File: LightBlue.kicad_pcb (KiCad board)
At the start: 2 copper layers, 120 x 120 mm, 0 parts

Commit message: Initial layout with footprint placements
Signed-off-by: Stefan Agner <stefan@agner.ch>
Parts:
- added BT1: Battery_Cell, Battery:BatteryHolder_Keystone_1060_1x2032, F.Cu at (49.6, 90.2)
- added C1: 100n, Capacitor_SMD:C_0402_1005Metric, F.Cu at (92.4, 52.2)
- added C10: 18p, Capacitor_SMD:C_0402_1005Metric, F.Cu at (96.1, 50.2)
- added C11: 100n, Capacitor_SMD:C_0402_1005Metric, F.Cu at (92.6, 54.6)
- added C12: 10u, Capacitor_SMD:C_0805_2012Metric, F.Cu at (103.6, 51.6)
- added C13: 100n, Capacitor_SMD:C_0402_1005Metric, F.Cu at (103.1, 58.6)
- added C14: 100n/1kV, Capacitor_SMD:C_1206_3216Metric, F.Cu at (78.2, 37.4)
- added C15: 100u, Capacitor_Tantalum_SMD:CP_EIA-7343-31_Kemet-D, F.Cu at (83.6, 44.0)
- added C16: 10u, Capacitor_SMD:C_0805_2012Metric, F.Cu at (77.8, 62.9)
- added C17: 10u, Capacitor_SMD:C_0805_2012Metric, F.Cu at (103.6, 49.4)
- added C18: 100n, Capacitor_SMD:C_0402_1005Metric, F.Cu at (81.5, 62.1)
- added C19: 100n, Capacitor_SMD:C_0402_1005Metric, F.Cu at (119.9, 58.0)
- added C2: 100n, Capacitor_SMD:C_0402_1005Metric, F.Cu at (95.4, 58.2)
- added C20: 10u, Capacitor_SMD:C_0805_2012Metric, F.Cu at (119.3, 53.5)
- added C21: 100n, Capacitor_SMD:C_0402_1005Metric, F.Cu at (119.9, 56.0)
- added C22: 10u, Capacitor_SMD:C_0805_2012Metric, F.Cu at (123.7, 56.5)
- added C23: 2u2/25V, Capacitor_SMD:C_0402_1005Metric, F.Cu at (110.4, 56.5)
- added C24: 2u2/25V, Capacitor_SMD:C_0402_1005Metric, F.Cu at (107.9, 56.5)
- added C25: 100n, Capacitor_SMD:C_0402_1005Metric, F.Cu at (117.0, 56.0)
- added C26: 100n, Capacitor_SMD:C_0402_1005Metric, F.Cu at (108.6, 46.2)
- added C27: 100n, Capacitor_SMD:C_0402_1005Metric, F.Cu at (117.0, 58.0)
- added C28: 100n, Capacitor_SMD:C_0402_1005Metric, F.Cu at (75.6, 57.0)
- added C29: 100n/1kV, Capacitor_SMD:C_1206_3216Metric, F.Cu at (62.3, 55.3)
- added C3: 100n, Capacitor_SMD:C_0402_1005Metric, F.Cu at (99.6, 52.6)
- added C30: 100n, Capacitor_SMD:C_0402_1005Metric, F.Cu at (138.4, 111.0)
- added C31: 100n, Capacitor_SMD:C_0402_1005Metric, F.Cu at (136.0, 136.0)
- added C32: 100n, Capacitor_SMD:C_0402_1005Metric, F.Cu at (135.3, 111.0)
- added C33: 33u/35V, Capacitor_Tantalum_SMD:CP_EIA-7343-31_Kemet-D, F.Cu at (6.74, 22.9)
- added C34: 33u/35V, Capacitor_Tantalum_SMD:CP_EIA-7343-31_Kemet-D, F.Cu at (-9.36, 35.5)
- added C35: 33u/35V, Capacitor_Tantalum_SMD:CP_EIA-7343-31_Kemet-D, F.Cu at (-10.3, 43.3)
- added C36: 10u/35V, Capacitor_SMD:C_0805_2012Metric, F.Cu at (6.24, 33.4)
- added C37: 33u/35V, Capacitor_Tantalum_SMD:CP_EIA-7343-31_Kemet-D, F.Cu at (-3.15, 22.9)
- added C38: 10u/35V, Capacitor_SMD:C_0805_2012Metric, F.Cu at (-3.17, 40.0)
- added C39: 100n/35V, Capacitor_SMD:C_0402_1005Metric, F.Cu at (-12.4, 54.8)
- added C4: 100n, Capacitor_SMD:C_0402_1005Metric, F.Cu at (99.6, 57.4)
- added C40: 100n/35V, Capacitor_SMD:C_0402_1005Metric, F.Cu at (-19.3, 62.5)
- added C41: 10n, Capacitor_SMD:C_0402_1005Metric, F.Cu at (-20.9, 65.5)
- added C42: 100n/35V, Capacitor_SMD:C_0402_1005Metric, F.Cu at (12.8, 31.5)
- added C43: 100n/35V, Capacitor_SMD:C_0402_1005Metric, F.Cu at (5.45, 37.9)
- added C44: 10n, Capacitor_SMD:C_0402_1005Metric, F.Cu at (16.6, 28.5)
- added C45: 47p, Capacitor_SMD:C_0402_1005Metric, F.Cu at (9.90, 33.5)
- added C46: 1n2, Capacitor_SMD:C_0402_1005Metric, F.Cu at (-5.80, 49.2)
- added C47: 47p, Capacitor_SMD:C_0402_1005Metric, F.Cu at (9.90, 31.5)
- added C48: 1n2, Capacitor_SMD:C_0402_1005Metric, F.Cu at (-12.4, 56.7)
- added C49: 47p, Capacitor_SMD:C_0402_1005Metric, F.Cu at (-23.7, 65.5)
- added C5: 1u, Capacitor_SMD:C_0402_1005Metric, F.Cu at (92.8, 58.4)
- added C50: 47p, Capacitor_SMD:C_0402_1005Metric, F.Cu at (-1.05, 44.4)
- added C51: 100n, Capacitor_SMD:C_0402_1005Metric, F.Cu at (-1.05, 42.5)
- added C52: 100n, Capacitor_SMD:C_0402_1005Metric, F.Cu at (-23.7, 67.4)
- added C53: 10u, Capacitor_SMD:C_0805_2012Metric, F.Cu at (3.99, 27.4)
- added C54: 10u, Capacitor_SMD:C_0805_2012Metric, F.Cu at (12.9, 29.1)
- added C55: 10u, Capacitor_SMD:C_0805_2012Metric, F.Cu at (8.44, 27.4)
- added C56: 10u, Capacitor_SMD:C_0805_2012Metric, F.Cu at (-18.5, 60.0)
- added C57: 10u, Capacitor_SMD:C_0805_2012Metric, F.Cu at (6.24, 30.4)
- added C58: 100u, Capacitor_Tantalum_SMD:CP_EIA-7343-31_Kemet-D, F.Cu at (-20.2, 49.1)
- added C59: 10u, Capacitor_SMD:C_0805_2012Metric, F.Cu at (-22.9, 60.0)
- added C6: 1u, Capacitor_SMD:C_0402_1005Metric, F.Cu at (97.8, 58.4)
- added C60: 100u, Capacitor_Tantalum_SMD:CP_EIA-7343-31_Kemet-D, F.Cu at (-3.15, 28.8)
- added C61: 100u, Capacitor_Tantalum_SMD:CP_EIA-7343-31_Kemet-D, F.Cu at (-20.2, 43.3)
- added C62: 100n, Capacitor_SMD:C_0402_1005Metric, F.Cu at (67.0, 140.5)
- added C63: 1u/35V, Capacitor_SMD:C_0402_1005Metric, F.Cu at (52.0, 138.5)
- added C64: 100n/35v, Capacitor_SMD:C_0402_1005Metric, F.Cu at (60.0, 138.5)
- added C65: 100n, Capacitor_SMD:C_0402_1005Metric, F.Cu at (72.1, 106.1)
- added C66: 1u, Capacitor_SMD:C_0402_1005Metric, F.Cu at (102.8, 137.9)
- added C67: 100n, Capacitor_SMD:C_0402_1005Metric, F.Cu at (113.0, 139.6)
- added C68: 100n, Capacitor_SMD:C_0402_1005Metric, F.Cu at (102.8, 140.4)
- added C69: 10u, Capacitor_SMD:C_0805_2012Metric, F.Cu at (130.8, 55.6)
- added C7: 100n, Capacitor_SMD:C_0402_1005Metric, F.Cu at (90.4, 59.2)
- added C70: 2n2/100V, Capacitor_SMD:C_0805_2012Metric, F.Cu at (190.7, 78.6)
- added C71: 1n/100V, Capacitor_SMD:C_0805_2012Metric, F.Cu at (182.1, 83.9)
- added C72: 1n/100V, Capacitor_SMD:C_0805_2012Metric, F.Cu at (200.3, 68.2)
- added C73: 47n/100V, Capacitor_SMD:C_0805_2012Metric, F.Cu at (209.3, 60.2)
- added C74: 100n/100V, Capacitor_SMD:C_0805_2012Metric, F.Cu at (182.1, 86.9)
- added C75: 100n/100V, Capacitor_SMD:C_0805_2012Metric, F.Cu at (215.3, 52.5)
- added C76: 100n/100V, Capacitor_SMD:C_0805_2012Metric, F.Cu at (194.1, 74.6)
- added C77: 100n/100V, Capacitor_SMD:C_0805_2012Metric, F.Cu at (209.3, 57.2)
- added C78: 100n/100V, Capacitor_SMD:C_0805_2012Metric, F.Cu at (176.2, 90.6)
- added C79: 100n/100V, Capacitor_SMD:C_0805_2012Metric, F.Cu at (200.3, 71.2)
- added C8: 4u7, Capacitor_SMD:C_0402_1005Metric, F.Cu at (99.6, 55.0)
- added C80: 47u/63V, Capacitor_SMD:C_0805_2012Metric, F.Cu at (186.6, 83.2)
- added C81: 2u2/100V, Capacitor_SMD:C_0805_2012Metric, F.Cu at (203.2, 63.6)
- added C82: 2u2/100V, Capacitor_SMD:C_0805_2012Metric, F.Cu at (187.8, 51.3)
- added C83: 47p/100V, Capacitor_SMD:C_0805_2012Metric, F.Cu at (223.6, 46.1)
- added C84: 2u2/100V, Capacitor_SMD:C_0805_2012Metric, F.Cu at (217.8, 49.5)
- added C85: 47n/100V, Capacitor_SMD:C_0805_2012Metric, F.Cu at (215.3, 55.5)
- added C86: 68n/100V, Capacitor_SMD:C_0805_2012Metric, F.Cu at (173.4, 95.2)
- added C87: 1n, Capacitor_SMD:C_0402_1005Metric, F.Cu at (184.3, 89.7)
- added C88: 1u, Capacitor_SMD:C_0402_1005Metric, F.Cu at (184.3, 91.6)
- added C89: 1n, Capacitor_SMD:C_0402_1005Metric, F.Cu at (188.7, 85.7)
- added C9: 18p, Capacitor_SMD:C_0402_1005Metric, F.Cu at (90.9, 49.7)
- added C90: 22n, Capacitor_SMD:C_0402_1005Metric, F.Cu at (197.3, 78.2)
- added C91: 100p, Capacitor_SMD:C_0402_1005Metric, F.Cu at (211.3, 62.7)
- added C92: 100u/35V, Capacitor_Tantalum_SMD:CP_EIA-7343-31_Kemet-D, F.Cu at (170.7, 78.5)
- added C93: 33u/35V, Capacitor_Tantalum_SMD:CP_EIA-7343-31_Kemet-D, F.Cu at (202.3, 40.9)
- added D1: LED_Small, LED_SMD:LED_0603_1608Metric, F.Cu at (120.8, 146.0)
- added D10: B2100-13-F, Diode_SMD:D_SMB, F.Cu at (192.3, 64.3)
- added D11: B2100-13-F, Diode_SMD:D_SMB, F.Cu at (169.9, 84.2)
- added D12: B2100-13-F, Diode_SMD:D_SMB, F.Cu at (194.8, 52.5)
- added D13: B2100-13-F, Diode_SMD:D_SMB, F.Cu at (203.2, 51.8)
- added D14: B2100-13-F, Diode_SMD:D_SMB, F.Cu at (211.4, 40.7)
- added D15: B2100-13-F, Diode_SMD:D_SMB, F.Cu at (184.0, 64.3)
- added D16: B2100-13-F, Diode_SMD:D_SMB, F.Cu at (211.4, 46.2)
- added D17: SMBJ58A-13-F, Diode_SMD:D_SMB, F.Cu at (179.8, 79.7)
- added D18: B3100-13-F, Diode_SMD:D_SMC, F.Cu at (185.2, 57.6)
- added D19: BAT41ZFILM, Diode_SMD:D_SOD-123, F.Cu at (177.0, 87.5)
- added D2: B3100-13-F, Diode_SMD:D_SMC, F.Cu at (-19.8, 36.5)
- added D20: BAT41ZFILM, Diode_SMD:D_SOD-123, F.Cu at (186.9, 75.5)
- added D21: BAT41ZFILM, Diode_SMD:D_SOD-123, F.Cu at (218.5, 46.3)
- added D22: BAT41ZFILM, Diode_SMD:D_SOD-123, F.Cu at (210.2, 50.7)
- added D23: BAT41ZFILM, Diode_SMD:D_SOD-123, F.Cu at (177.0, 84.1)
- added D24: B3100-13-F, Diode_SMD:D_SMC, F.Cu at (171.2, 71.7)
- added D25: BAT54S-7-F, Package_TO_SOT_SMD:SOT-23, F.Cu at (198.8, 64.4)
- added D26: BAT41ZFILM, Diode_SMD:D_SOD-123, F.Cu at (210.2, 54.0)
- added D27: BZX84C18, Diode_SMD:D_SOT-23_ANK, F.Cu at (186.2, 79.4)
- added D3: LED Green, LED_SMD:LED_0603_1608Metric, F.Cu at (94.5, 146.0)
- added D4: LED Red, LED_SMD:LED_0603_1608Metric, F.Cu at (89.0, 146.0)
- added D5: BAT54C-7-F, Package_TO_SOT_SMD:SOT-23, F.Cu at (68.6, 109.1)
- added D6: LTST-C19HE1WT, LED_SMD:LED_LiteOn_LTST-C19HE1WT, F.Cu at (101.0, 146.0)
- added D7: LTST-C19HE1WT, LED_SMD:LED_LiteOn_LTST-C19HE1WT, F.Cu at (113.9, 145.8)
- added D8: LTST-C19HE1WT, LED_SMD:LED_LiteOn_LTST-C19HE1WT, F.Cu at (107.9, 145.8)
- added D9: B2100-13-F, Diode_SMD:D_SMB, F.Cu at (194.8, 58.1)
- added F1: Polyfuse_Small, Fuse:Fuse_1206_3216Metric, F.Cu at (131.0, 45.4)
- added FB1: 300R/3A, Resistor_SMD:R_0805_2012Metric, F.Cu at (-23.0, 63.0)
- added FB2: 300R/2A, Resistor_SMD:R_0805_2012Metric, F.Cu at (180.6, 90.6)
- added FB3: 300R/2A, Resistor_SMD:R_0805_2012Metric, F.Cu at (207.6, 63.6)
- added FID1: Fiducial, Fiducial:Fiducial_1mm_Mask2mm, F.Cu at (160.0, 21.0)
- added FID2: Fiducial, Fiducial:Fiducial_1mm_Mask2mm, F.Cu at (166.0, 21.0)
- added FID3: Fiducial, Fiducial:Fiducial_1mm_Mask2mm, F.Cu at (170.0, 21.1)
- added FID4: Fiducial, Fiducial:Fiducial_1mm_Mask2mm, F.Cu at (175.9, 21.1)
- added FID5: Fiducial, Fiducial:Fiducial_1mm_Mask2mm, F.Cu at (161.9, 26.0)
- added FID6: Fiducial, Fiducial:Fiducial_1mm_Mask2mm, F.Cu at (175.9, 24.6)
- added FID7: Fiducial, Fiducial:Fiducial_1mm_Mask2mm, F.Cu at (169.0, 26.0)
- added FID8: Fiducial, Fiducial:Fiducial_1mm_Mask2mm, F.Cu at (165.4, 26.0)
- added H1: MountingHole, MountingHole:MountingHole_2.7mm_M2.5, F.Cu at (40.0, 40.0)
- added H2: MountingHole, MountingHole:MountingHole_2.7mm_M2.5, F.Cu at (140.0, 40.0)
- added H3: MountingHole, MountingHole:MountingHole_2.7mm_M2.5, F.Cu at (140.0, 141.0)
- added H4: MountingHole, MountingHole:MountingHole_2.7mm_M2.5, F.Cu at (40.0, 140.0)
- added HS1: Heatsink, LightBlue:Heatsink_60x60mm_2xFixation3.2mm, F.Cu at (83.2, 50.1)
- added J1: Conn_02x05_Odd_Even, Connector_PinHeader_2.54mm:PinHeader_2x05_P2.54mm_Vertical, F.Cu at (40.3, 107.0)
- added J10: Bus_M.2_Socket_M, LightBlue:TE_2199230_Bus_M.2_M_H4.2mm_P0.5mm_2280_Horizontal, F.Cu at (142.4, 123.2)
- added J11: Barrel_Jack, Connector_BarrelJack:BarrelJack_Horizontal, F.Cu at (50.2, 42.2)
- added J12: Micro_SD_Card_Det, Connector_Card:microSD_HC_Molex_104031-0811, F.Cu at (140.2, 52.4)
- added J2: HDMI_A_2.0, LightBlue:HDMI_A_Molex_2086588131_Horizontal, F.Cu at (127.0, 38.0)
- added J3: USB_C_Receptacle_USB2.0, Connector_USB:USB_C_Receptacle_HRO_TYPE-C-31-M-12, F.Cu at (85.0, 32.5)
- added J4: USB_A_Stacked, Connector_USB:USB_A_Wuerth_61400826021_Horizontal_Stacked, F.Cu at (102.5, 44.0)
- added J5: SiLabs Mini Debug, Connector_PinHeader_1.27mm:PinHeader_2x05_P1.27mm_Vertical_SMD, F.Cu at (54.0, 122.7)
- added J6: Conn_Coaxial, Connector_Coaxial:U.FL_Hirose_U.FL-R-SMT-1_Vertical, F.Cu at (33.2, 107.2)
- added J7: Conn_02x04_Odd_Even, Connector_PinHeader_2.54mm:PinHeader_2x05_P2.54mm_Vertical, F.Cu at (34.0, 131.0)
- added J8: AudioJack3, LightBlue:Jack_3.5mm_CUI_SJ2-35953A-SMT_Horizontal, F.Cu at (113.5, 36.0)
- added J9: RJ45_LINK-PP_LPJG0926HENL_Horizontal, LightBlue:RJ45_LINK-PP_LPJG0926HENL_Horizontal, F.Cu at (70.2, 48.5)
- added L1: 3u3, Inductor_SMD:L_Bourns_SRN6045TA, F.Cu at (-11.3, 50.0)
- added L2: 3u3, Inductor_SMD:L_Bourns_SRN6045TA, F.Cu at (15.7, 23.8)
- added L3: 3u3, Inductor_SMD:L_Bourns_SRN6045TA, F.Cu at (203.1, 58.4)
- added L4: 2m2, LightBlue:L_Bourns-SDR1006, F.Cu at (191.5, 43.8)
- added L5: 10u, Inductor_SMD:L_Bourns_SRR1260, F.Cu at (172.8, 60.8)
- added M1: Fan_4pin, Connector:FanPinHeader_1x04_P2.54mm_Vertical, F.Cu at (51.0, 133.0)
- added Q1: FDMC2523P, Package_SO:Vishay_PowerPAK_1212-8_Single, F.Cu at (168.5, 96.0)
- added Q2: FDMS86255, Package_TO_SOT_SMD:TDSON-8-1, F.Cu at (219.7, 41.3)
- added Q3: CSD17510Q5A, Package_TO_SOT_SMD:TDSON-8-1, F.Cu at (187.8, 70.4)
- added Q4: BCX56, Package_TO_SOT_SMD:SOT-89-3, F.Cu at (195.0, 70.1)
- added Q5: CSD17510Q5A, Package_TO_SOT_SMD:TDSON-8-1, F.Cu at (169.9, 90.3)
- added R1: 10k, Resistor_SMD:R_0402_1005Metric, F.Cu at (116.6, 102.4)
- added R10: 12k/1%, Resistor_SMD:R_0402_1005Metric, F.Cu at (87.0, 49.6)
- added R11: 10k, Resistor_SMD:R_0402_1005Metric, F.Cu at (98.4, 49.6)
- added R12: 5k1, Resistor_SMD:R_0402_1005Metric, F.Cu at (86.4, 39.0)
- added R13: 5k1, Resistor_SMD:R_0402_1005Metric, F.Cu at (81.4, 39.0)
- added R14: 0R, Resistor_SMD:R_0402_1005Metric, F.Cu at (80.2, 39.0)
- added R15: 0R, Resistor_SMD:R_0402_1005Metric, F.Cu at (113.9, 57.0)
- added R16: 470R, Resistor_SMD:R_0402_1005Metric, F.Cu at (112.3, 44.0)
- added R17: 470R, Resistor_SMD:R_0402_1005Metric, F.Cu at (109.4, 44.0)
- added R18: 470Ω, Resistor_SMD:R_0402_1005Metric, F.Cu at (66.6, 54.6)
- added R19: 470Ω, Resistor_SMD:R_0402_1005Metric, F.Cu at (75.6, 55.0)
- added R2: 1k, Resistor_SMD:R_0402_1005Metric, F.Cu at (81.8, 58.2)
- added R20: 0R, Resistor_SMD:R_0402_1005Metric, F.Cu at (72.7, 59.1)
- added R21: 1k, Resistor_SMD:R_0402_1005Metric, F.Cu at (120.8, 143.6)
- added R22: 10R, Resistor_SMD:R_0402_1005Metric, F.Cu at (-5.78, 47.2)
- added R23: 10R, Resistor_SMD:R_0402_1005Metric, F.Cu at (21.2, 21.0)
- added R24: 20k, Resistor_SMD:R_0402_1005Metric, F.Cu at (-3.94, 42.5)
- added R25: 20k, Resistor_SMD:R_0402_1005Metric, F.Cu at (-3.94, 44.5)
- added R26: 47k/1%, Resistor_SMD:R_0402_1005Metric, F.Cu at (0.51, 39.1)
- added R27: 15k/1%, Resistor_SMD:R_0402_1005Metric, F.Cu at (-15.3, 54.8)
- added R28: 12k/1%, Resistor_SMD:R_0402_1005Metric, F.Cu at (5.47, 35.9)
- added R29: 2k2/1%, Resistor_SMD:R_0402_1005Metric, F.Cu at (-15.3, 56.8)
- added R3: 2k2/1%, Resistor_SMD:R_0402_1005Metric, F.Cu at (144.0, 102.1)
- added R30: 1k, Resistor_SMD:R_0402_1005Metric, F.Cu at (94.5, 143.5)
- added R31: 1k, Resistor_SMD:R_0402_1005Metric, F.Cu at (89.0, 144.0)
- added R32: 10k, Resistor_SMD:R_0402_1005Metric, F.Cu at (70.5, 140.5)
- added R33: 10k, Resistor_SMD:R_0402_1005Metric, F.Cu at (55.5, 138.5)
- added R34: 10k, Resistor_SMD:R_0402_1005Metric, F.Cu at (83.6, 141.4)
- added R35: 100R, Resistor_SMD:R_0402_1005Metric, F.Cu at (67.6, 105.6)
- added R36: 10k, Resistor_SMD:R_0402_1005Metric, F.Cu at (130.6, 58.2)
- added R37: 31R6/1%, Resistor_SMD:R_0402_1005Metric, F.Cu at (219.0, 52.0)
- added R38: 60k4/1%, Resistor_SMD:R_0402_1005Metric, F.Cu at (213.0, 60.0)
- added R39: 237k/1%, Resistor_SMD:R_0402_1005Metric, F.Cu at (203.9, 70.1)
- added R4: 3k6, Resistor_SMD:R_0402_1005Metric, F.Cu at (144.0, 106.8)
- added R40: 49k9/1%, Resistor_SMD:R_0402_1005Metric, F.Cu at (194.4, 77.1)
- added R41: 0R, Resistor_SMD:R_0402_1005Metric, F.Cu at (180.0, 93.1)
- added R42: 25k5/1%, Resistor_SMD:R_0402_1005Metric, F.Cu at (190.2, 83.1)
- added R43: 110k, Resistor_SMD:R_0402_1005Metric, F.Cu at (194.4, 79.1)
- added R44: 10k, Resistor_SMD:R_0402_1005Metric, F.Cu at (227.3, 45.4)
- added R45: 42k2, Resistor_SMD:R_0402_1005Metric, F.Cu at (193.1, 81.1)
- added R46: 499k, Resistor_SMD:R_0402_1005Metric, F.Cu at (185.8, 87.7)
- added R47: 0R, Resistor_SMD:R_0402_1005Metric, F.Cu at (203.9, 66.1)
- added R48: 10k, Resistor_SMD:R_0402_1005Metric, F.Cu at (185.8, 85.7)
- added R49: 4R7, Resistor_SMD:R_0402_1005Metric, F.Cu at (215.9, 58.0)
- added R5: 2k2/1%, Resistor_SMD:R_0402_1005Metric, F.Cu at (144.6, 104.0)
- added R50: 2k49/1%, Resistor_SMD:R_0402_1005Metric, F.Cu at (221.9, 50.6)
- added R51: 2k/1%, Resistor_SMD:R_0402_1005Metric, F.Cu at (177.1, 93.1)
- added R52: 0R1, Resistor_SMD:R_0402_1005Metric, F.Cu at (177.1, 95.1)
- added R53: 511R/1%, Resistor_SMD:R_0402_1005Metric, F.Cu at (213.0, 58.0)
- added R54: 1k47, Resistor_SMD:R_0402_1005Metric, F.Cu at (221.9, 52.6)
- added R55: 10R, Resistor_SMD:R_0402_1005Metric, F.Cu at (219.0, 54.0)
- added R56: 49R9, Resistor_SMD:R_0402_1005Metric, F.Cu at (228.2, 43.4)
- added R57: 22k, Resistor_SMD:R_0402_1005Metric, F.Cu at (225.3, 43.4)
- added R58: 5R1, Resistor_SMD:R_0402_1005Metric, F.Cu at (222.8, 48.6)
- added R59: 499R, Resistor_SMD:R_0402_1005Metric, F.Cu at (227.3, 47.4)
- added R6: 2k2/1%, Resistor_SMD:R_0402_1005Metric, F.Cu at (144.6, 108.4)
- added R60: 10k2/1%, Resistor_SMD:R_0402_1005Metric, F.Cu at (190.2, 81.1)
- added R61: 5R1, Resistor_SMD:R_0402_1005Metric, F.Cu at (203.9, 68.1)
- added R62: 4k99, Resistor_SMD:R_0402_1005Metric, F.Cu at (177.1, 97.1)
- added R63: 1k21/1%, Resistor_SMD:R_0402_1005Metric, F.Cu at (206.8, 66.1)
- added R7: 10k, Resistor_SMD:R_0402_1005Metric, F.Cu at (78.9, 60.2)
- added R8: 10k, Resistor_SMD:R_0402_1005Metric, F.Cu at (98.4, 51.0)
- added R9: 10k, Resistor_SMD:R_0402_1005Metric, F.Cu at (78.9, 58.2)
- added SW1: SW_DEBUG_MODE, Button_Switch_SMD:SW_SPDT_PCM12, F.Cu at (148.2, 106.2)
- added SW2: SW_RESET, Button_Switch_THT:SW_Tactile_SPST_Angled_PTS645Vx39-2LFS, F.Cu at (70.0, 148.0)
- added SW3: SW_RECOVERY, Button_Switch_SMD:SW_SPST_EVQP7C, F.Cu at (76.8, 32.3)
- added SW4: SW_POWER, Button_Switch_THT:SW_Tactile_SPST_Angled_PTS645Vx39-2LFS, F.Cu at (57.0, 148.0)
- added SW5: SW_USER, Button_Switch_THT:SW_Tactile_SPST_Angled_PTS645Vx39-2LFS, F.Cu at (82.0, 148.0)
- added T1: Transformer_Wurth_749119550, LightBlue:Transformer_Wuerth_749119550, F.Cu at (175.7, 45.9)
- added TP1: TestPoint, TestPoint:TestPoint_Pad_D2.0mm, F.Cu at (198.4, 75.2)
- added U1: RaspberryPi-CM4Lite, LightBlue:RaspberryPi-CM4, F.Cu at (122.0, 80.0)
- added U10: PCM5121PW, Package_SO:TSSOP-28_4.4x9.7mm_P0.65mm, F.Cu at (110.9, 51.0)
- added U11: TLV74033PDBVR, Package_TO_SOT_SMD:SOT-23-5, F.Cu at (118.9, 49.0)
- added U12: TPD4EUSB30, Package_SON:USON-10_2.5x1.0mm_P0.5mm, F.Cu at (60.9, 59.0)
- added U13: TPD4EUSB30, Package_SON:USON-10_2.5x1.0mm_P0.5mm, F.Cu at (72.7, 56.0)
- added U14: AP64501SP-13, Package_SO:SOIC-8-1EP_3.9x4.9mm_P1.27mm_EP2.95x4.9mm_Mask2.71x3.4mm_ThermalVias, F.Cu at (-0.21, 34.9)
- added U15: AP64501SP-13, Package_SO:SOIC-8-1EP_3.9x4.9mm_P1.27mm_EP2.95x4.9mm_Mask2.71x3.4mm_ThermalVias, F.Cu at (-20.9, 55.3)
- added U16: 74LVC07APW, Package_SO:TSSOP-14_4.4x5mm_P0.65mm, F.Cu at (77.2, 139.0)
- added U17: LP5569RTWR, Package_DFN_QFN:WQFN-24-1EP_4x4mm_P0.5mm_EP2.45x2.45mm, F.Cu at (108.0, 139.6)
- added U18: PCF85063AT, Package_SO:SOIC-8_3.9x4.9mm_P1.27mm, F.Cu at (68.6, 100.6)
- added U19: RT9742GGJ5, Package_TO_SOT_SMD:SOT-23-5, F.Cu at (131.0, 51.2)
- added U2: CP2102N-Axx-xQFN24, Package_DFN_QFN:QFN-24-1EP_4x4mm_P0.5mm_EP2.6x2.6mm, F.Cu at (88.2, 77.8)
- added U20: TPS23734, LightBlue:Texas_VQFN-47-2EP_5x7mm_P0.4mm_ThermalVias, F.Cu at (180.2, 72.3)
- added U21: TCMT1107, Package_SO:SOP-4_4.4x2.6mm_P1.27mm, F.Cu at (202.1, 45.9)
- added U22: TL431CDBVR, Package_TO_SOT_SMD:SOT-23-5, F.Cu at (226.4, 40.1)
- added U3: FSUSB42MUX, Package_SO:MSOP-10_3x3mm_P0.5mm, F.Cu at (88.0, 70.8)
- added U4: FSUSB42MUX, Package_SO:MSOP-10_3x3mm_P0.5mm, F.Cu at (88.0, 63.8)
- added U5: TPD4EUSB30, Package_SON:USON-10_2.5x1.0mm_P0.5mm, F.Cu at (84.2, 39.2)
- added U6: USB2422, Package_DFN_QFN:QFN-24-1EP_4x4mm_P0.5mm_EP2.6x2.6mm, F.Cu at (95.8, 54.6)
- added U7: AP2171W, Package_TO_SOT_SMD:SOT-23-5, F.Cu at (103.0, 54.8)
- added U8: TPD4EUSB30, Package_SON:USON-10_2.5x1.0mm_P0.5mm, F.Cu at (98.8, 47.2)
- added U9: SiliconLabs-MGM210P, LightBlue:SiliconLabs_MGM210P, F.Cu at (37.5, 117.1)
- added Y1: 24MHz, Crystal:Crystal_SMD_3225-4Pin_3.2x2.5mm, F.Cu at (93.3, 48.7)
- added Y2: X32K768S301, Crystal:Crystal_SMD_3215-2Pin_3.2x1.5mm, F.Cu at (61.6, 103.6)
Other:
- outline, holes or cut-outs redrawn

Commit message: [WIP] PCB commit
Signed-off-by: Dominik Sliwa <dominik@sliwa.io>
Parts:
- removed C7: 100n, Capacitor_SMD:C_0402_1005Metric
- D18, D24: value B3100-13-F -> B2100-13-F; footprint Diode_SMD:D_SMC -> Diode_SMD:D_SMB
- R14, R20: footprint Resistor_SMD:R_0402_1005Metric -> Resistor_SMD:R_1206_3216Metric
- R52: footprint Resistor_SMD:R_0402_1005Metric -> Resistor_SMD:R_0805_2012Metric
- SW3: footprint Button_Switch_SMD:SW_SPST_EVQP7C -> Button_Switch_SMD:SW_SPST_B3U-3100P-B
- TP1: footprint TestPoint:TestPoint_Pad_D2.0mm -> TestPoint:TestPoint_Pad_D1.0mm
- moved R58 193.1 mm to (38.8, 107.1), turned to -90 degrees
- moved R59 188.8 mm to (47.6, 105.3), turned to 180 degrees
- moved R55 187.2 mm to (38.4, 103.0)
- moved C75 181.3 mm to (35.1, 72.1)
- moved Q2 181.1 mm to (41.2, 71.9), turned to -90 degrees
- moved C84 180.7 mm to (39.3, 77.4), turned to 90 degrees
- moved C83 180.7 mm to (43.7, 63.2), turned to 90 degrees
- moved R50 179.4 mm to (43.2, 65.9), turned to -90 degrees
- moved C58 175.9 mm to (131.7, 137.9), turned to 180 degrees
- moved D21 174.6 mm to (47.7, 82.6), turned to -90 degrees
- moved C77 174.5 mm to (35.1, 68.1)
- moved R44 173.5 mm to (54.4, 59.7), turned to 180 degrees
- moved R56 172.5 mm to (62.6, 92.0), turned to 180 degrees
- moved FID8 172.0 mm to (42.3, 146.1)
- moved R49 171.3 mm to (45.0, 69.3), turned to 180 degrees
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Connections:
- R3 pad 2: /USB/UBS_OTG_ID -> /CM4/CM4_USB_OTG_ID
- R5 pad 1: /USB/UBS_OTG_ID -> /CM4/CM4_USB_OTG_ID
- U12 pad 4: /CM4/ETH.TD2+ -> /CM4/ETH.TD2-
- U12 pad 5: /CM4/ETH.TD2- -> /CM4/ETH.TD2+
- U13 pad 4: /CM4/ETH.TD4+ -> /CM4/ETH.TD4-
- U13 pad 5: /CM4/ETH.TD4- -> /CM4/ETH.TD4+
- U3 pad 3: /USB/UBS-C.D+ -> /USB/USB-C.D+
- U4 pad 2: /USB/UBS_OTG_ID -> /CM4/CM4_USB_OTG_ID
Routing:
- net GND: track 0.00 -> 195.2 mm, vias 0 -> 125
- net +12V: track 0.00 -> 137.4 mm
- net /CM4/ETH.TD3+: track 0.00 -> 87.9 mm, vias 0 -> 2
- net /CM4/ETH.TD3-: track 0.00 -> 87.3 mm, vias 0 -> 2
- net /CM4/PCIe.CLK+: track 0.00 -> 85.2 mm, vias 0 -> 2
- net /CM4/ETH.TD4+: track 0.00 -> 85.0 mm, vias 0 -> 2
- net /CM4/ETH.TD4-: track 0.00 -> 85.0 mm, vias 0 -> 2
- net /CM4/PCIe.CLK-: track 0.00 -> 84.8 mm, vias 0 -> 2
- net /CM4/PCIe.TX+: track 0.00 -> 81.1 mm, vias 0 -> 2
- net /CM4/PCIe.TX-: track 0.00 -> 80.6 mm, vias 0 -> 2
- net /CM4/ETH.TD2-: track 0.00 -> 80.2 mm
- net GNDA: track 0.00 -> 80.1 mm, vias 0 -> 3
- net /CM4/PCIe.RX+: track 0.00 -> 78.7 mm, vias 0 -> 2
- net /CM4/PCIe.RX-: track 0.00 -> 78.2 mm, vias 0 -> 2
- net /CM4/ETH.TD1-: track 0.00 -> 75.0 mm
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- added copper zone on F.Cu, net +12V
- added copper zone on F.Cu, net +3.3VP
- added copper zone on F.Cu, net +5V
- added copper zone on In1.Cu, net GND
- added copper zone on In2.Cu, net GND
- added copper zone on In1.Cu, net GND1
- added copper zone on In2.Cu, net GND1
- added copper zone on B.Cu, net VSS
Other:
- copper layers 2 -> 4

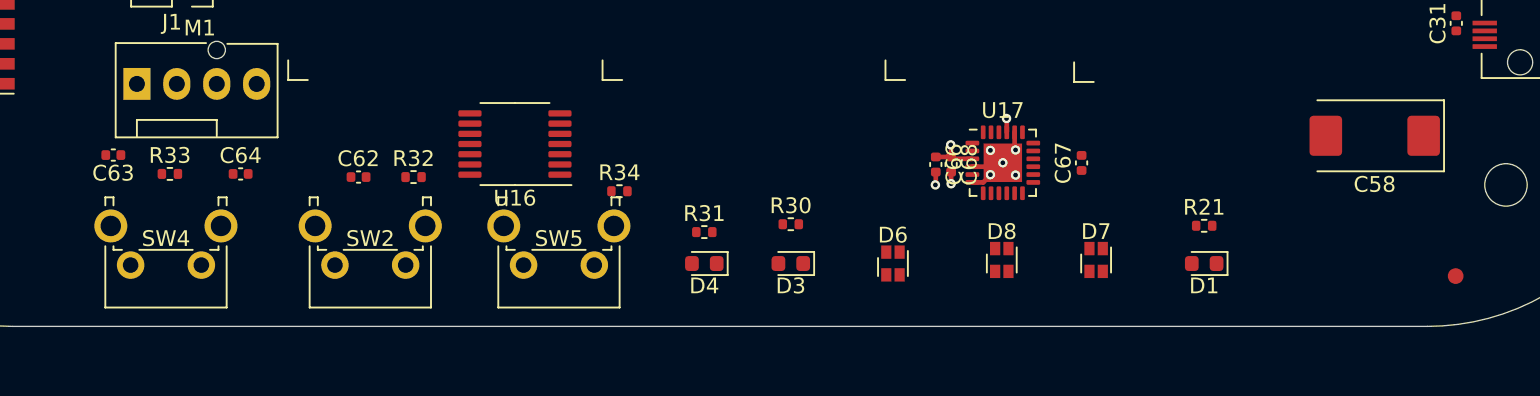
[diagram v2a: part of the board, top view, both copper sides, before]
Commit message: Add Light Pipes
Add Light Pipes and densify front a bit.

Signed-off-by: Stefan Agner <stefan@agner.ch>
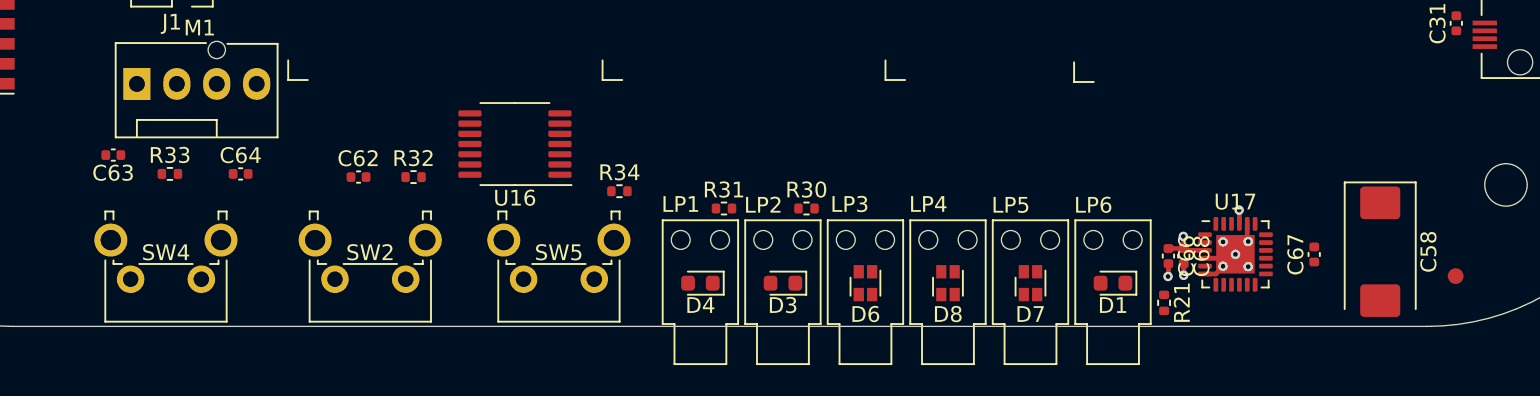
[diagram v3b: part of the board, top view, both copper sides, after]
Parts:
- added LP1: LightPipe, LightBlue:Lightpipe_Bivar-SLP3-150-100-F, F.Cu at (88.8, 144.5)
- added LP2: LightPipe, LightBlue:Lightpipe_Bivar-SLP3-150-100-F, F.Cu at (94.0, 144.5)
- added LP3: LightPipe, LightBlue:Lightpipe_Bivar-SLP3-150-100-F, F.Cu at (99.2, 144.5)
- added LP4: LightPipe, LightBlue:Lightpipe_Bivar-SLP3-150-100-F, F.Cu at (104.5, 144.5)
- added LP5: LightPipe, LightBlue:Lightpipe_Bivar-SLP3-150-100-F, F.Cu at (109.8, 144.5)
- added LP6: LightPipe, LightBlue:Lightpipe_Bivar-SLP3-150-100-F, F.Cu at (115.0, 144.5)
- moved C66 15.9 mm to (118.5, 145.5)
- moved U17 15.9 mm to (122.8, 145.4)
- moved C67 15.9 mm to (127.8, 145.4)
- moved C68 15.9 mm to (119.5, 145.5)
- moved C58 7.38 mm to (132.0, 145.2), turned to -90 degrees
- moved D1 5.93 mm to (115.0, 147.2)
- moved R21 5.52 mm to (118.2, 148.5), turned to -90 degrees
- moved D7 4.43 mm to (109.8, 147.2)
- moved D8 3.73 mm to (104.5, 147.2)
- moved D6 2.15 mm to (99.2, 147.2)
- moved R31 1.95 mm to (90.2, 142.5)
- moved R30 1.41 mm to (95.5, 142.5)
- moved D3 1.35 mm to (94.0, 147.2)
- moved D4 1.27 mm to (88.8, 147.2)
- moved SW2 0.90 mm to (70.0, 147.0)
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
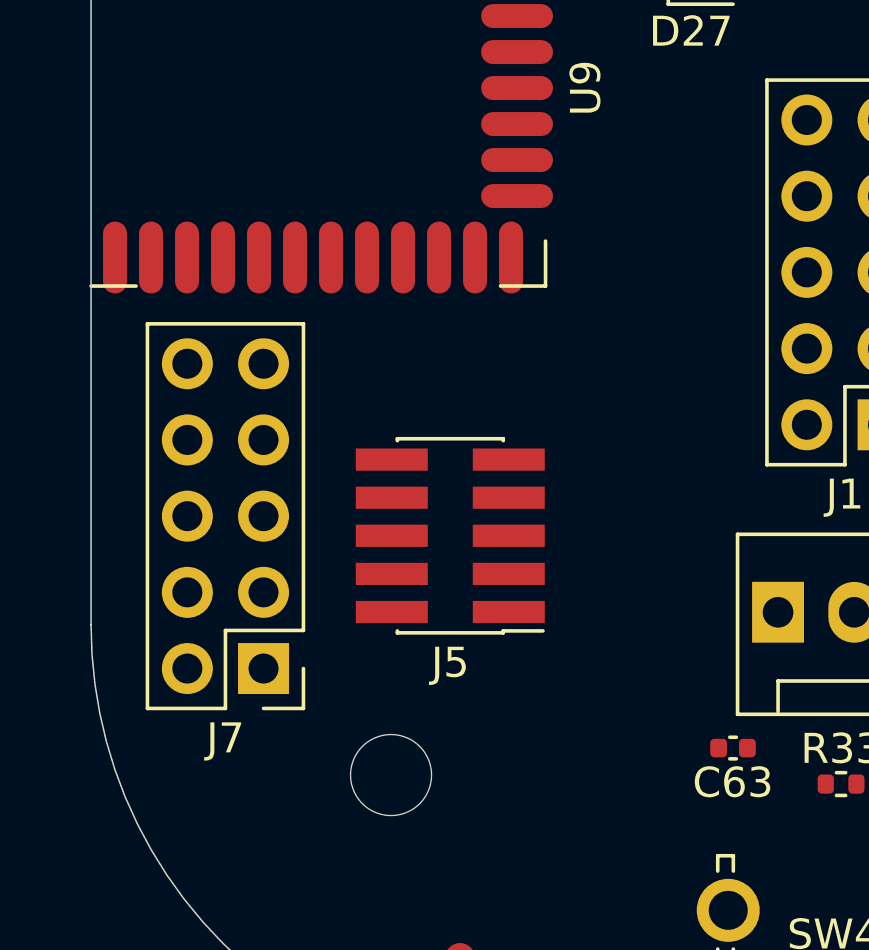
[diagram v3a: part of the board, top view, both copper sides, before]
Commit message: Define 3D models and offsets for KiCad footprints
Signed-off-by: Stefan Agner <stefan@agner.ch>
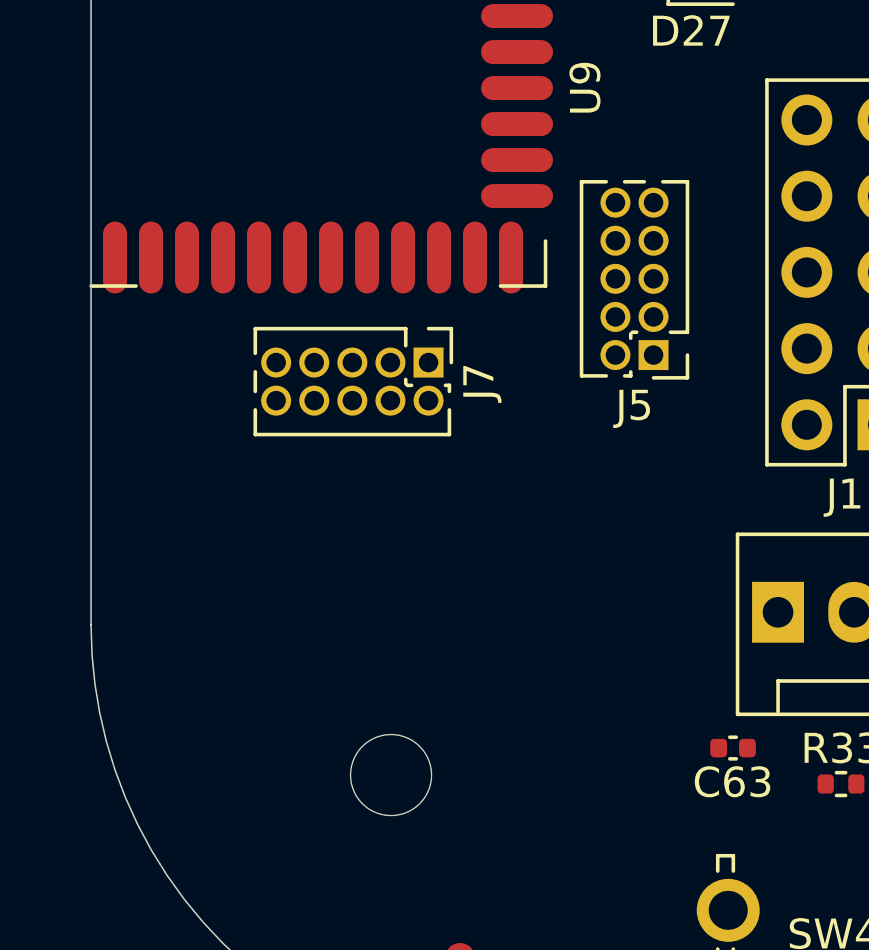
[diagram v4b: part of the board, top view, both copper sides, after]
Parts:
- J5: footprint Connector_PinHeader_1.27mm:PinHeader_2x05_P1.27mm_Vertical_SMD -> Connector_PinHeader_1.27mm:PinHeader_2x05_P1.27mm_Vertical
- J7: footprint Connector_PinHeader_2.54mm:PinHeader_2x05_P2.54mm_Vertical -> Connector_PinHeader_1.27mm:PinHeader_2x05_P1.27mm_Vertical
- moved J7 11.6 mm to (41.2, 126.2), turned to -90 degrees
- moved J5 9.07 mm to (48.8, 126.0)
